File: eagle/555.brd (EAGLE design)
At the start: 50.8 x 50.8 mm, 7 parts, among them P1 1k

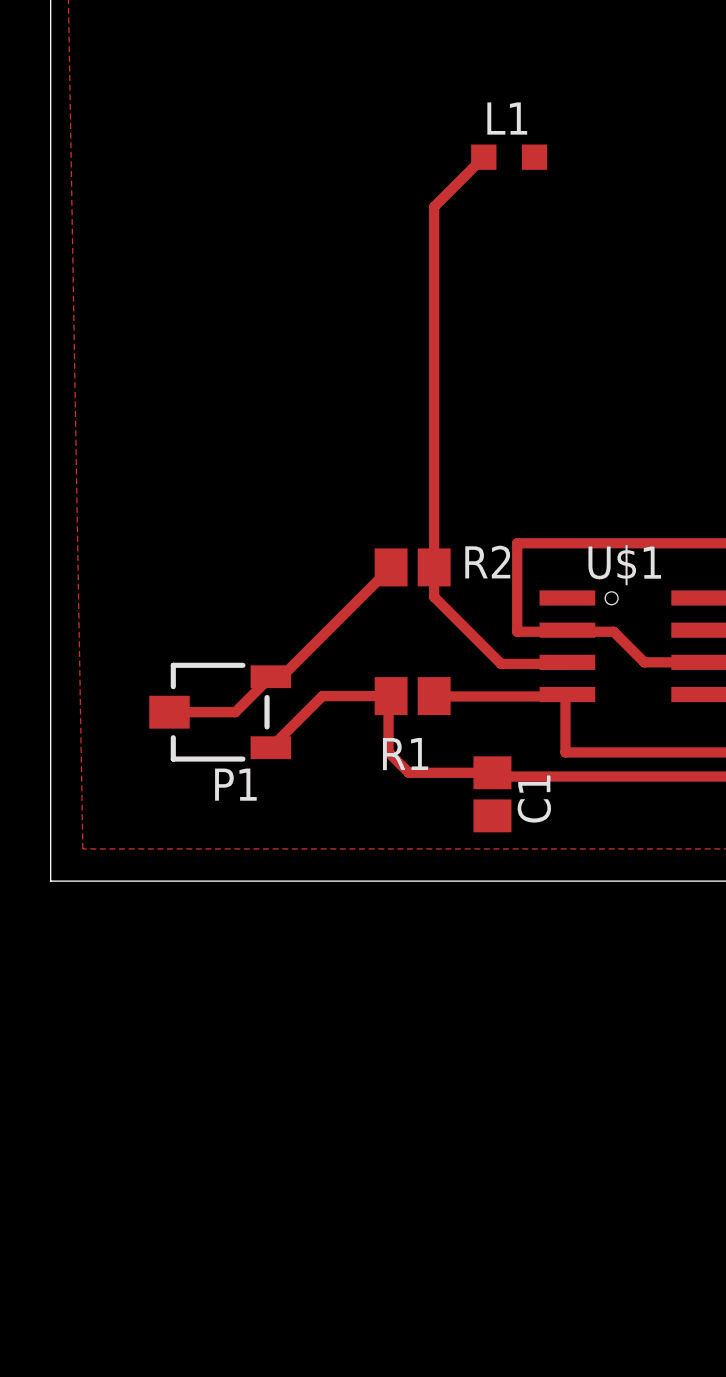
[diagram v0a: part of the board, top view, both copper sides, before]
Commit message: mofified 555 timer schematic and layout
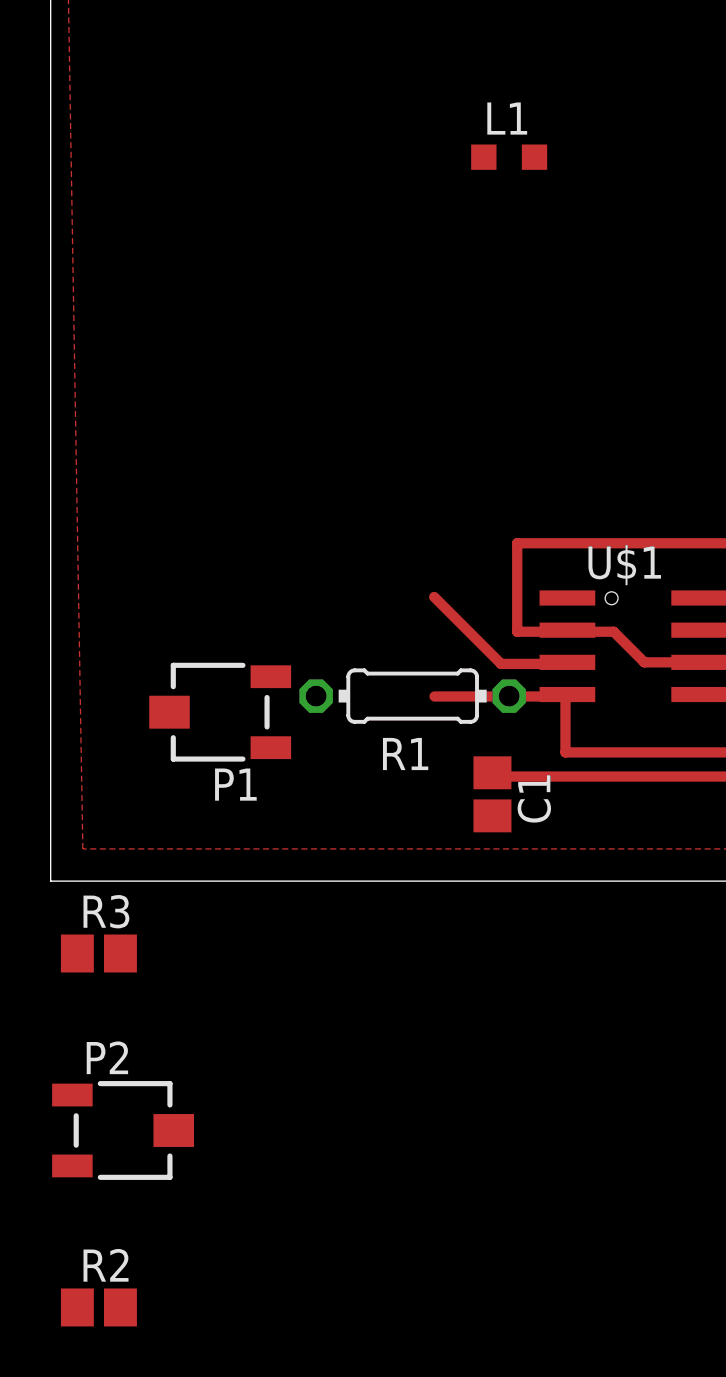
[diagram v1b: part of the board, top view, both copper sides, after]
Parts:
- added P2: 1k, potentiometer:3223J
- added R3: 1.8k, resistor:R0805
- C1: value 2.2nF -> 1nF
- C2: value 0.01uF -> 0.1uF
- R1: device resistor:R0805 -> resistor:0204/7
- moved R2 31.7 mm to (1.91, -16.8)
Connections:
- new net N$4: C1.1, R3.1, U$1.2, U$1.6
- new net N$5: P2.2, P2.3, R3.2
- new net N$6: P1.3, R1.1
- new net N$8: L1.1, R2.2
- net GND: no longer U$1.7
- net N$1: now also P2.1, U$1.7; no longer C1.1, R1.2, U$1.2, U$1.6
- net N$2: now also R2.1; no longer L1.1, R2.2
- net N$3: no longer P1.3, R2.1
- net VCC: now also R1.2; no longer R1.1
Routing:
- net N$1: track 67.7 -> 0.00 mm
- net N$4: track 0.00 -> 55.1 mm
- net N$2: track 24.6 -> 6.38 mm
- net N$3: track 11.1 -> 0.00 mm
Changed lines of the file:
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@@
 </autorouter>
 <elements>
-<element name="R1" library="resistor" package="R0805" value="100k" x="14.2875" y="7.3025" smashed="yes" rot="R180">
+<element name="R1" library="resistor" package="0204/7" value="100k" x="14.2875" y="7.3025" smashed="yes" rot="R180">
 <attribute name="NAME" x="15.0495" y="5.6515" size="1.27" layer="25" rot="R180"/>
 </element>
-<element name="C1" library="resistor" package="C0805" value="2.2nF" x="17.437859375" y="3.425378125" smashed="yes" rot="R270">
+<element name="C1" library="resistor" package="C0805" value="1nF" x="17.437859375" y="3.425378125" smashed="yes" rot="R270">
 <attribute name="NAME" x="18.453859375" y="4.314378125" size="1.27" layer="25" rot="R270"/>
 </element>
-<element name="C2" library="resistor" package="C0805" value="0.01uF" x="30.48" y="7.3025" smashed="yes">
+<element name="C2" library="resistor" package="C0805" value="0.1uF" x="30.48" y="7.3025" smashed="yes">
 <attribute name="NAME" x="29.591" y="8.3185" size="1.27" layer="25"/>
-</element>
-<element name="R2" library="resistor" package="R0805" value="1.8k" x="14.2875" y="12.3825" smashed="yes">
-<attribute name="NAME" x="16.210621875" y="11.94541875" size="1.27" layer="25"/>
 </element>
 <element name="L1" library="resistor" package="L2012C" value="" x="18.0975" y="28.575"/>
 <element name="U$1" library="ece510_library" package="TLC555CRD" value="TLC555CDR" x="23.346465625" y="9.6193625" rot="R270"/>
 <element name="P1" library="potentiometer" package="3223J" value="1k" x="6.690428125" y="6.6675" rot="R180"/>
+<element name="R3" library="resistor" package="R0805" value="1.8k" x="1.905" y="-2.8575"/>
+<element name="P2" library="potentiometer" package="3223J" value="1k" x="2.8575" y="-9.8425"/>
+<element name="R2" library="resistor" package="R0805" value="1.8k" x="1.905" y="-16.8275"/>
 </elements>
 <signals>
@@
 <contactref element="U$1" pad="1"/>
 <contactref element="C1" pad="2"/>
-<contactref element="U$1" pad="7"/>
-<wire x1="20.396465625" y1="11.1743625" x2="17.437859375" y2="2.575378125" width="0" layer="19" extent="1-1"/>
-</signal>
-<signal name="N$1">
-<contactref element="R1" pad="2"/>
-<contactref element="U$1" pad="2"/>
-<contactref element="U$1" pad="6"/>
-<contactref element="C1" pad="1"/>
-<wire x1="25.596465625" y1="8.6343625" x2="23.4331375" y2="8.6343625" width="0.4064" layer="1"/>
-<wire x1="23.4331375" y1="8.6343625" x2="22.225" y2="9.8425" width="0.4064" layer="1"/>
-<wire x1="22.225" y1="9.8425" x2="20.458328125" y2="9.8425" width="0.4064" layer="1"/>
-<wire x1="20.458328125" y1="9.8425" x2="20.396465625" y2="9.9043625" width="0.4064" layer="1"/>
-<contactref element="P1" pad="1"/>
-<wire x1="13.4375" y1="7.3025" x2="10.725428125" y2="7.3025" width="0.4064" layer="1"/>
-<wire x1="10.725428125" y1="7.3025" x2="8.690428125" y2="5.2675" width="0.4064" layer="1"/>
-<wire x1="17.437859375" y1="4.275378125" x2="14.139621875" y2="4.275378125" width="0.4064" layer="1"/>
-<wire x1="14.139621875" y1="4.275378125" x2="13.335" y2="5.08" width="0.4064" layer="1"/>
-<wire x1="13.335" y1="5.08" x2="13.335" y2="7.2" width="0.4064" layer="1"/>
-<wire x1="13.335" y1="7.2" x2="13.4375" y2="7.3025" width="0.4064" layer="1"/>
-<wire x1="20.458328125" y1="9.8425" x2="18.415" y2="9.8425" width="0.4064" layer="1"/>
-<wire x1="18.415" y1="9.8425" x2="18.415" y2="13.335" width="0.4064" layer="1"/>
-<wire x1="18.415" y1="13.335" x2="34.925" y2="13.335" width="0.4064" layer="1"/>
-<wire x1="34.925" y1="13.335" x2="35.56" y2="12.7" width="0.4064" layer="1"/>
-<wire x1="35.56" y1="12.7" x2="35.56" y2="4.1275" width="0.4064" layer="1"/>
-<wire x1="35.56" y1="4.1275" x2="17.5857375" y2="4.1275" width="0.4064" layer="1"/>
-<wire x1="17.5857375" y1="4.1275" x2="17.437859375" y2="4.275378125" width="0.4064" layer="1"/>
+<wire x1="20.396465625" y1="11.1743625" x2="31.33" y2="7.3025" width="0" layer="19" extent="1-1"/>
+<wire x1="17.437859375" y1="2.575378125" x2="20.396465625" y2="11.1743625" width="0" layer="19" extent="1-1"/>
 </signal>
 <signal name="N$2">
 <contactref element="U$1" pad="3"/>
-<contactref element="R2" pad="2"/>
-<contactref element="L1" pad="1"/>
-<wire x1="15.1375" y1="12.3825" x2="15.1375" y2="11.215" width="0.4064" layer="1"/>
 <wire x1="15.1375" y1="11.215" x2="17.78" y2="8.5725" width="0.4064" layer="1"/>
 <wire x1="17.78" y1="8.5725" x2="20.334603125" y2="8.5725" width="0.4064" layer="1"/>
 <wire x1="20.334603125" y1="8.5725" x2="20.396465625" y2="8.6343625" width="0.4064" layer="1"/>
-<wire x1="15.1375" y1="12.3825" x2="15.1375" y2="26.615" width="0.4064" layer="1"/>
-<wire x1="15.1375" y1="26.615" x2="17.0975" y2="28.575" width="0.4064" layer="1"/>
-</signal>
-<signal name="N$3">
 <contactref element="R2" pad="1"/>
-<contactref element="P1" pad="3"/>
-<contactref element="P1" pad="2"/>
-<wire x1="4.690428125" y1="6.6675" x2="7.290428125" y2="6.6675" width="0.4064" layer="1"/>
-<wire x1="7.290428125" y1="6.6675" x2="8.690428125" y2="8.0675" width="0.4064" layer="1"/>
-<wire x1="8.690428125" y1="8.0675" x2="9.1225" y2="8.0675" width="0.4064" layer="1"/>
-<wire x1="9.1225" y1="8.0675" x2="13.4375" y2="12.3825" width="0.4064" layer="1"/>
+<wire x1="1.055" y1="-16.8275" x2="17.78" y2="8.5725" width="0" layer="19" extent="1-1"/>
 </signal>
 <signal name="VCC">
 <contactref element="U$1" pad="4"/>
-<contactref element="R1" pad="1"/>
 <contactref element="U$1" pad="8"/>
 <wire x1="25.596465625" y1="11.1743625" x2="33.655" y2="11.1743625" width="0.4064" layer="1"/>
@@
 <wire x1="20.32" y1="7.287896875" x2="20.396465625" y2="7.3643625" width="0.4064" layer="1"/>
 <wire x1="20.32" y1="7.287896875" x2="15.152103125" y2="7.287896875" width="0.4064" layer="1"/>
-<wire x1="15.152103125" y1="7.287896875" x2="15.1375" y2="7.3025" width="0.4064" layer="1"/>
 <wire x1="20.32" y1="5.08" x2="20.32" y2="7.287896875" width="0.4064" layer="1"/>
+<contactref element="R1" pad="2"/>
+<wire x1="10.4775" y1="7.3025" x2="15.152103125" y2="7.287896875" width="0" layer="19" extent="1-1"/>
 </signal>
 <signal name="N$7">
@@
 <wire x1="29.63" y1="7.3643625" x2="29.63" y2="7.3025" width="0.4064" layer="1"/>
 </signal>
+<signal name="N$4">
+<contactref element="U$1" pad="6"/>
+<wire x1="25.596465625" y1="8.6343625" x2="23.4331375" y2="8.6343625" width="0.4064" layer="1"/>
+<wire x1="23.4331375" y1="8.6343625" x2="22.225" y2="9.8425" width="0.4064" layer="1"/>
+<wire x1="22.225" y1="9.8425" x2="20.458328125" y2="9.8425" width="0.4064" layer="1"/>
+<wire x1="20.458328125" y1="9.8425" x2="18.415" y2="9.8425" width="0.4064" layer="1"/>
+<wire x1="18.415" y1="9.8425" x2="18.415" y2="13.335" width="0.4064" layer="1"/>
+<wire x1="18.415" y1="13.335" x2="34.925" y2="13.335" width="0.4064" layer="1"/>
+<wire x1="34.925" y1="13.335" x2="35.56" y2="12.7" width="0.4064" layer="1"/>
+<wire x1="35.56" y1="12.7" x2="35.56" y2="4.1275" width="0.4064" layer="1"/>
+<wire x1="35.56" y1="4.1275" x2="17.5857375" y2="4.1275" width="0.4064" layer="1"/>
+<contactref element="U$1" pad="2"/>
+<contactref element="C1" pad="1"/>
+<contactref element="R3" pad="1"/>
+<wire x1="20.458328125" y1="9.8425" x2="20.396465625" y2="9.9043625" width="0" layer="19" extent="1-1"/>
+<wire x1="17.437859375" y1="4.275378125" x2="17.5857375" y2="4.1275" width="0" layer="19" extent="1-1"/>
+<wire x1="1.055" y1="-2.8575" x2="17.437859375" y2="4.275378125" width="0" layer="19" extent="1-1"/>
+</signal>
+<signal name="N$1">
+<contactref element="U$1" pad="7"/>
+<contactref element="P2" pad="1"/>
+<contactref element="P1" pad="1"/>
+<wire x1="8.690428125" y1="5.2675" x2="25.596465625" y2="9.9043625" width="0" layer="19" extent="1-1"/>
+<wire x1="0.8575" y1="-8.4425" x2="8.690428125" y2="5.2675" width="0" layer="19" extent="1-1"/>
+</signal>
+<signal name="N$5">
+<contactref element="R3" pad="2"/>
+<contactref element="P2" pad="3"/>
+<contactref element="P2" pad="2"/>
+<wire x1="4.8575" y1="-9.8425" x2="0.8575" y2="-11.2425" width="0" layer="19" extent="1-1"/>
+<wire x1="2.755" y1="-2.8575" x2="4.8575" y2="-9.8425" width="0" layer="19" extent="1-1"/>
+</signal>
+<signal name="N$3">
+<contactref element="P1" pad="2"/>
+</signal>
+<signal name="N$6">
+<contactref element="R1" pad="1"/>
+<contactref element="P1" pad="3"/>
+<wire x1="8.690428125" y1="8.0675" x2="18.0975" y2="7.3025" width="0" layer="19" extent="1-1"/>
+</signal>
+<signal name="N$8">
+<contactref element="R2" pad="2"/>
+<contactref element="L1" pad="1"/>
+<wire x1="2.755" y1="-16.8275" x2="17.0975" y2="28.575" width="0" layer="19" extent="1-1"/>
+</signal>
 </signals>
